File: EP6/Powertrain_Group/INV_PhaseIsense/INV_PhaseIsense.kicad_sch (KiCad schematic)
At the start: 4 parts, among them IC1 LZSR_80-TP, IC2 LZSR_80-TP, IC3 LZSR_80-TP, J1 to INV_Mainboard_TI

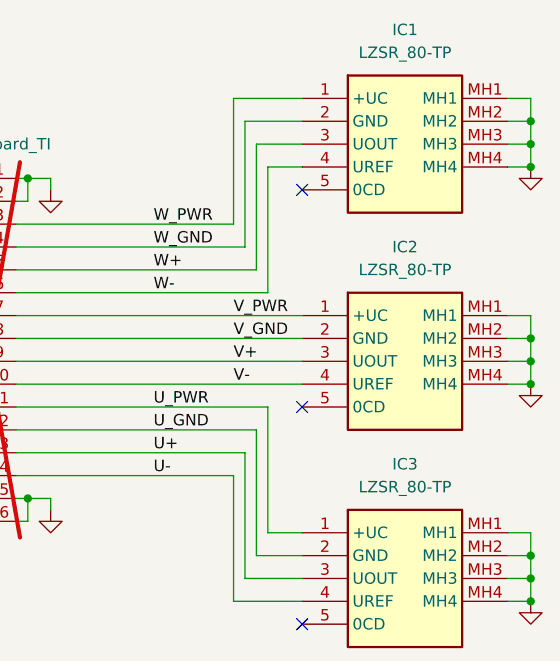
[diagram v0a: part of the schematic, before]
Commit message: update INV_PhaseIsense to V1.1
offset connector to mainboard by 6 mm to better match power module
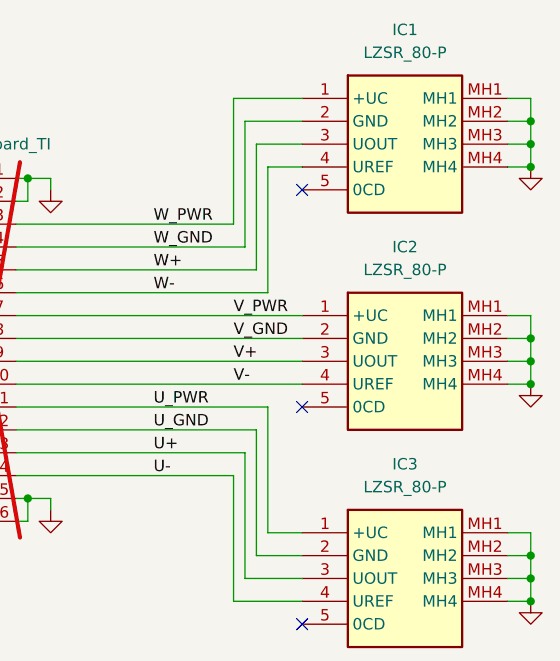
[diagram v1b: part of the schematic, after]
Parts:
- IC1, IC2, IC3: value LZSR_80-TP -> LZSR_80-P; footprint nturt_kicad_lib_EP6:LZSR80P -> LZSR80P; symbol nturt_kicad_lib_EP6:LZSR_80-TP -> nturt_kicad_lib_EP6:LZSR_80-P
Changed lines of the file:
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@@
 	(title_block
 		(title "INV_PhaseIsense")
-		(date "2025-02-19")
-		(rev "1.0")
+		(date "2025-03-07")
+		(rev "1.1")
 		(company "NTURacing")
 		(comment 1 "郭哲明 Jack Kuo")
@@
 	)
 	(symbol
-		(lib_id "nturt_kicad_lib_EP6:LZSR_80-TP")
+		(lib_id "nturt_kicad_lib_EP6:LZSR_80-P")
 		(at 88.9 69.85 0)
 		(unit 1)
@@
 			)
 		)
-		(property "Value" "LZSR_80-TP"
+		(property "Value" "LZSR_80-P"
 			(at 100.33 64.77 0)
 			(effects
@@
 			)
 		)
-		(property "Footprint" "nturt_kicad_lib_EP6:LZSR80P"
+		(property "Footprint" "LZSR80P"
 			(at 115.57 164.77 0)
 			(effects
@@
 	)
 	(symbol
-		(lib_id "nturt_kicad_lib_EP6:LZSR_80-TP")
+		(lib_id "nturt_kicad_lib_EP6:LZSR_80-P")
 		(at 88.9 93.98 0)
 		(unit 1)
@@
 			)
 		)
-		(property "Value" "LZSR_80-TP"
+		(property "Value" "LZSR_80-P"
 			(at 100.33 88.9 0)
 			(effects
@@
 			)
 		)
-		(property "Footprint" "nturt_kicad_lib_EP6:LZSR80P"
+		(property "Footprint" "LZSR80P"
 			(at 115.57 188.9 0)
 			(effects
@@
 	)
 	(symbol
-		(lib_id "nturt_kicad_lib_EP6:LZSR_80-TP")
+		(lib_id "nturt_kicad_lib_EP6:LZSR_80-P")
 		(at 88.9 45.72 0)
 		(unit 1)
@@
 			)
 		)
-		(property "Value" "LZSR_80-TP"
+		(property "Value" "LZSR_80-P"
 			(at 100.33 40.64 0)
 			(effects
@@
 			)
 		)
-		(property "Footprint" "nturt_kicad_lib_EP6:LZSR80P"
+		(property "Footprint" "LZSR80P"
 			(at 115.57 140.64 0)
 			(effects

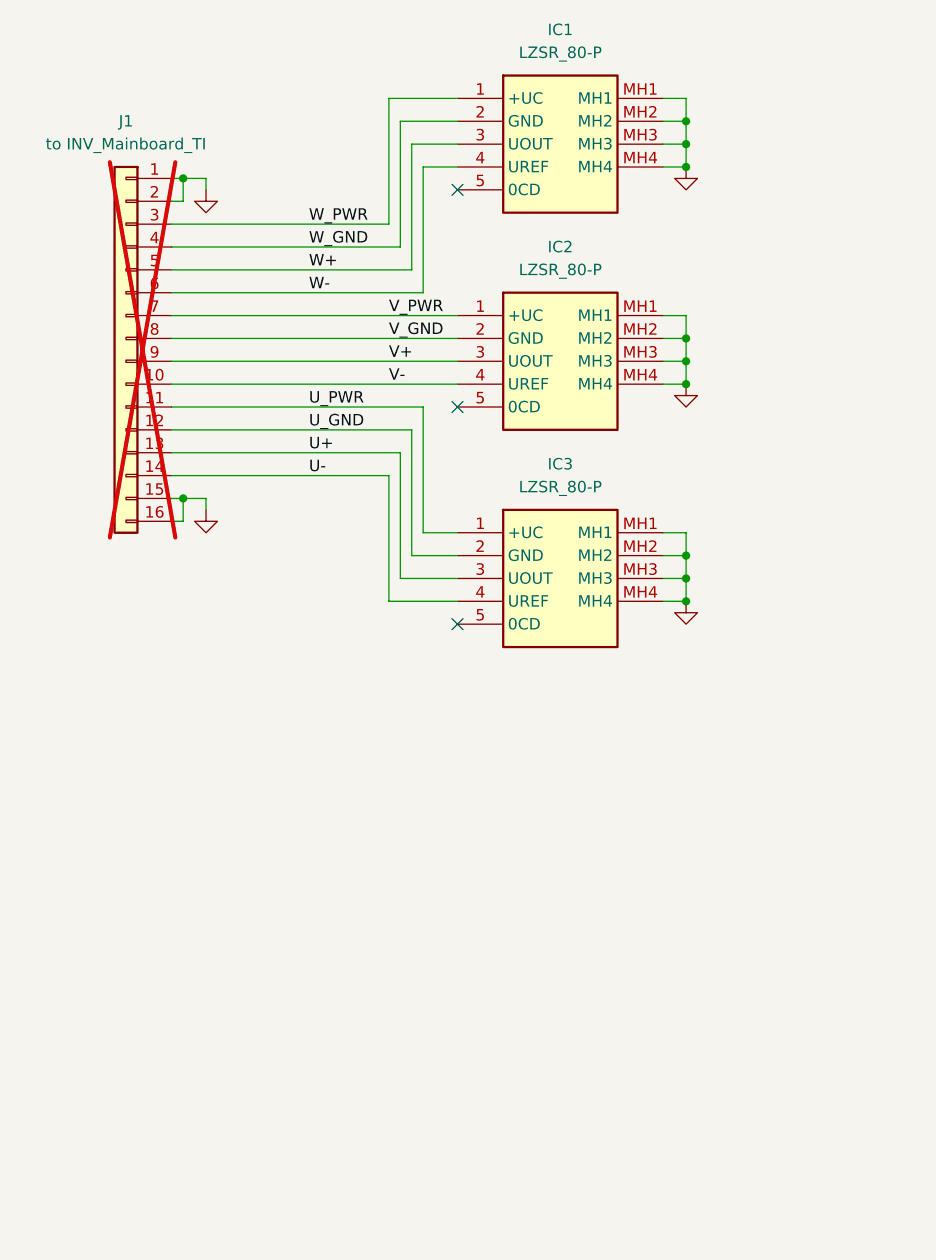
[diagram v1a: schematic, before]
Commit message: update INV_PhaseIsense to V1.2
V1.2
shift connector up about 6mm and right 6mm exactly (back to where V1.0 is)
for better bus assembly
add mounting hole for more sturdy mounting
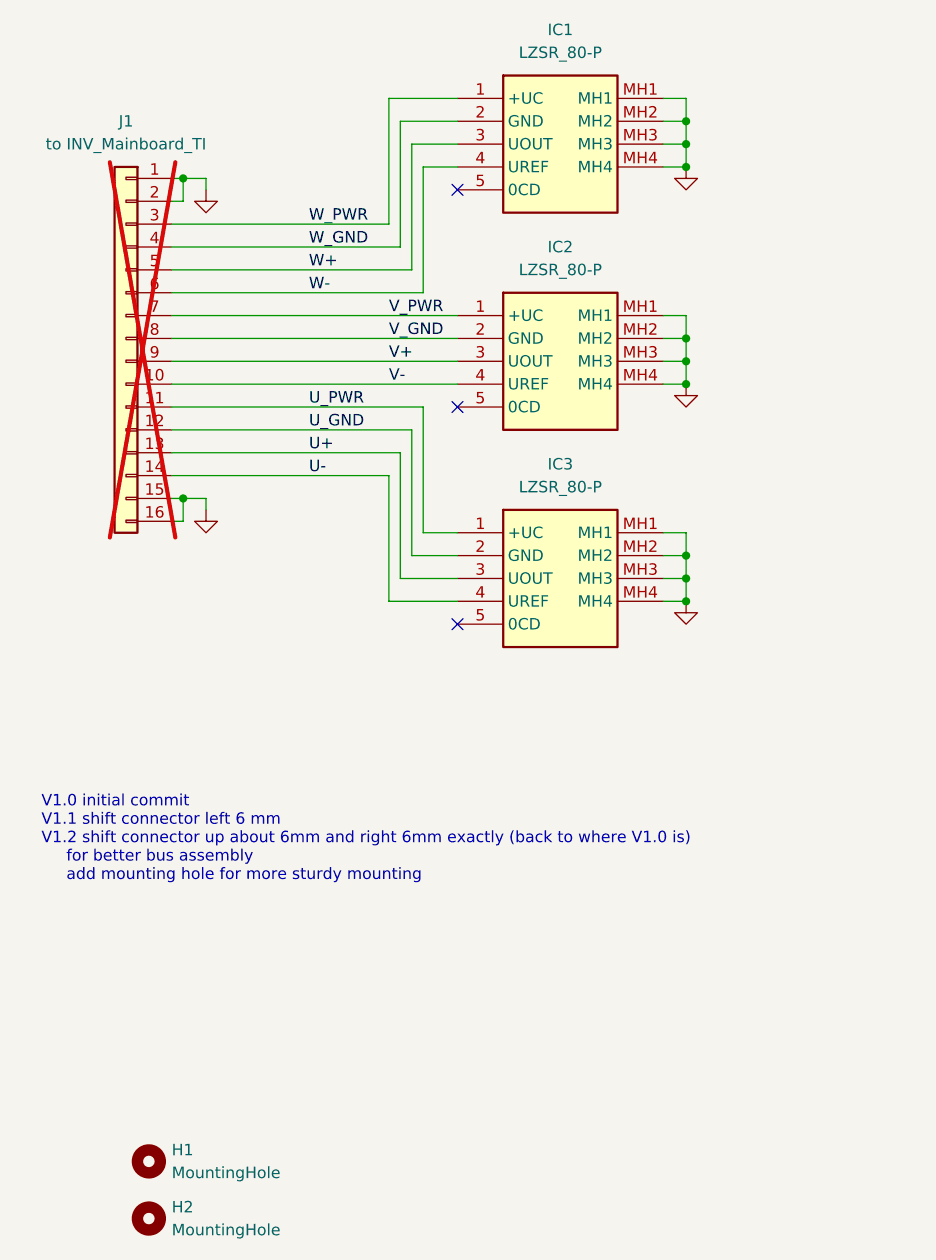
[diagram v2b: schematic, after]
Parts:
- added H1, H2: MountingHole, MountingHole:MountingHole_3.2mm_M3, symbol Mechanical:MountingHole
- IC1, IC2, IC3: footprint LZSR80P -> nturt_kicad_lib_EP6:LZSR80P
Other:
- note added: "V1.0 initial commit V1.1 shift connector left 6 mm V1.2 shift connector up about 6mm and right 6mm exactly (back to where V1.0 is) for better bus assembly add mounting hole for more sturdy mounting"
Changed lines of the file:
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@@
 	(title_block
 		(title "INV_PhaseIsense")
-		(date "2025-03-07")
-		(rev "1.1")
+		(date "2025-05-10")
+		(rev "1.2")
 		(company "NTURacing")
 		(comment 1 "郭哲明 Jack Kuo")
@@
 			(width 0)
 			(type default)
+		)
+	)
+	(text "V1.0 initial commit\nV1.1 shift connector left 6 mm\nV1.2 shift connector up about 6mm and right 6mm exactly (back to where V1.0 is)\n     for better bus assembly\n     add mounting hole for more sturdy mounting "
+		(exclude_from_sim no)
+		(at 42.672 123.19 0)
+		(effects
+			(font
+				(size 1.27 1.27)
+			)
+			(justify left top)
 		)
 	)
@@
 			)
 		)
-		(property "Footprint" "LZSR80P"
+		(property "Footprint" "nturt_kicad_lib_EP6:LZSR80P"
 			(at 115.57 164.77 0)
 			(effects
@@
 			)
 		)
-		(property "Footprint" "LZSR80P"
+		(property "Footprint" "nturt_kicad_lib_EP6:LZSR80P"
 			(at 115.57 188.9 0)
 			(effects
@@
 				(path "/c6725d55-5833-4586-96a2-48404258060f"
 					(reference "IC3")
+					(unit 1)
+				)
+			)
+		)
+	)
+	(symbol
+		(lib_id "Mechanical:MountingHole")
+		(at 54.61 163.83 0)
+		(unit 1)
+		(exclude_from_sim yes)
+		(in_bom no)
+		(on_board yes)
+		(dnp no)
+		(fields_autoplaced yes)
+		(property "Reference" "H1"
+			(at 57.15 162.5599 0)
+			(effects
+				(font
+					(size 1.27 1.27)
+				)
+				(justify left)
+			)
+		)
+		(property "Value" "MountingHole"
+			(at 57.15 165.0999 0)
+			(effects
+				(font
+					(size 1.27 1.27)
+				)
+				(justify left)
+			)
+		)
+		(property "Footprint" "MountingHole:MountingHole_3.2mm_M3"
+			(at 54.61 163.83 0)
+			(effects
+				(font
+					(size 1.27 1.27)
+				)
+				(hide yes)
+			)
+		)
+		(property "Datasheet" "~"
+			(at 54.61 163.83 0)
+			(effects
+				(font
+					(size 1.27 1.27)
+				)
+				(hide yes)
+			)
+		)
+		(property "Description" "Mounting Hole without connection"
+			(at 54.61 163.83 0)
+			(effects
+				(font
+					(size 1.27 1.27)
+				)
+				(hide yes)
+			)
+		)
+		(instances
+			(project ""
+				(path "/c6725d55-5833-4586-96a2-48404258060f"
+					(reference "H1")
 					(unit 1)
 				)
@@
 			)
 		)
-		(property "Footprint" "LZSR80P"
+		(property "Footprint" "nturt_kicad_lib_EP6:LZSR80P"
 			(at 115.57 140.64 0)
 			(effects
@@
 					(unit 1)
 				)
+			)
+		)
+	)
+	(symbol
+		(lib_id "Mechanical:MountingHole")
+		(at 54.61 170.18 0)
+		(unit 1)
+		(exclude_from_sim yes)
+		(in_bom no)
+		(on_board yes)
+		(dnp no)
+		(fields_autoplaced yes)
+		(property "Reference" "H2"
+			(at 57.15 168.9099 0)
+			(effects
+				(font
+					(size 1.27 1.27)
+				)
+				(justify left)
+			)
+		)
+		(property "Value" "MountingHole"
+			(at 57.15 171.4499 0)
+			(effects
+				(font
+					(size 1.27 1.27)
+				)
+				(justify left)
+			)
+		)
+		(property "Footprint" "MountingHole:MountingHole_3.2mm_M3"
+			(at 54.61 170.18 0)
+			(effects
+				(font
+					(size 1.27 1.27)
+				)
+				(hide yes)
+			)
+		)
+		(property "Datasheet" "~"
+			(at 54.61 170.18 0)
+			(effects
+				(font
+					(size 1.27 1.27)
+				)
+				(hide yes)
+			)
+		)
+		(property "Description" "Mounting Hole without connection"
+			(at 54.61 170.18 0)
+			(effects
+				(font
+					(size 1.27 1.27)
+				)
+				(hide yes)
+			)
+		)
+		(instances
+			(project "INV_PhaseIsense"
+				(path "/c6725d55-5833-4586-96a2-48404258060f"
+					(reference "H2")
+					(unit 1)
+				)
